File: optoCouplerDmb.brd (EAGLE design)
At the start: 46 x 43 mm, 19 parts, among them U1 6N137, U2 6N137

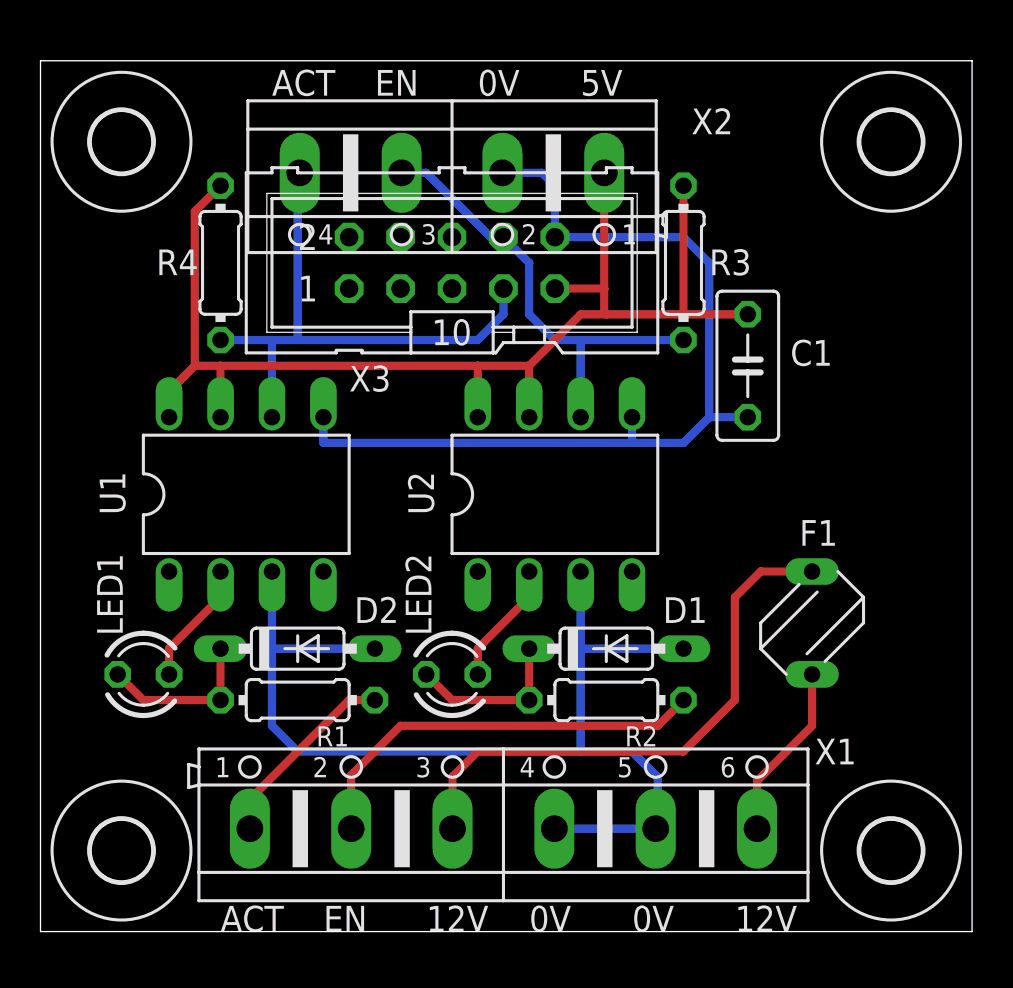
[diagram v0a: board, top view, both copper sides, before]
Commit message: resistors 10mm , added led
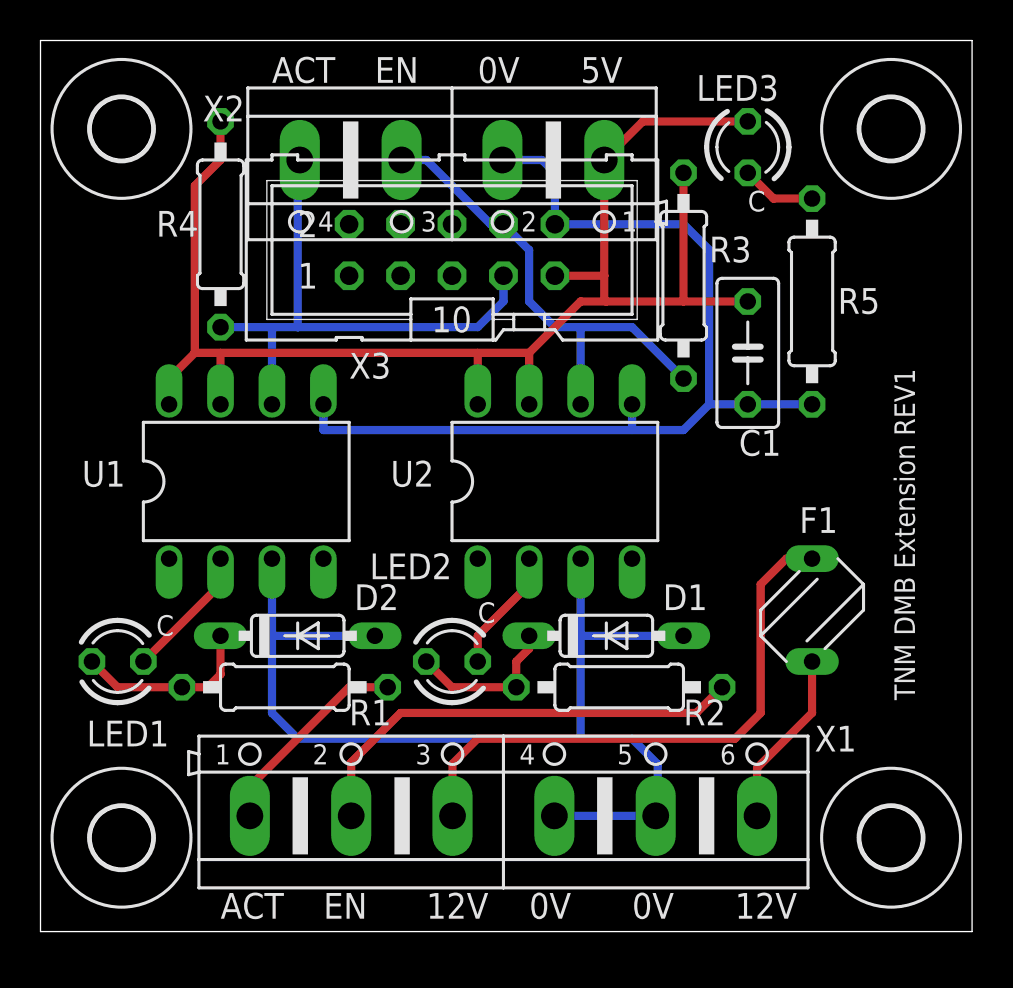
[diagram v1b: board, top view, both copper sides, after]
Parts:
- added LED3: (no value), led:LED3MM
- added R5: 1k, rcl:0207/10
- R1, R2, R3, R4: device rcl:0204/7 -> rcl:0207/10
- moved R4 1.90 mm to (8.89, 34.9)
- moved LED1 1.42 mm to (3.81, 13.3)
- moved R1 0.90 mm to (12.1, 12.1)
- moved R2 0.90 mm to (28.6, 12.1)
- moved R3 0.64 mm to (31.8, 32.4)
- moved LED2 0.64 mm to (20.3, 13.3)
- moved U1 0.64 mm to (10.2, 22.2)
- moved U2 0.64 mm to (25.4, 22.2)
- moved D1 0.63 mm to (27.9, 14.6)
- moved D2 0.63 mm to (12.7, 14.6)
- moved F1 0.63 mm to (38.1, 15.9)
- moved H1 0.63 mm to (42.0, 4.63)
- moved H2 0.63 mm to (4.00, 4.63)
- moved X1 0.63 mm to (22.9, 5.71)
- moved C1 0.63 mm to (34.9, 28.6)
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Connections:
- new net N$3: LED3.K, R5.2
- net GND: now also R5.1
- net VCC: now also LED3.A
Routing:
- net VCC: track 64.3 -> 74.7 mm
- net N$3: track 0.00 -> 3.70 mm
- net GND: track 45.2 -> 48.4 mm
- net ENABLE: track 20.6 -> 22.5 mm
- net OUT_ENABLE: track 22.6 -> 23.7 mm
- net N$1: track 8.15 -> 9.04 mm
- net 12VFUSED: track 27.5 -> 28.2 mm
- net ACTIVE: track 9.65 -> 10.3 mm
- net N$2: track 6.13 -> 6.66 mm
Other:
- board size 46 x 43 mm -> 46 x 44 mm
- board text added: "C"
- board text added: "TNM DMB Extension REV1"
